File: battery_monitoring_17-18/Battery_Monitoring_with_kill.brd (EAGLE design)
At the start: 50.8 x 127 mm, 57 parts, among them CON4 MOLEX_5566-2, CON5 S3B-PH-SM4-TB, CON6 S3B-PH-SM4-TB, U1 INA3221., U2 INA3221., U4 TEENSY_3.1_BASIC_2, U6 TCAN1042HVDR

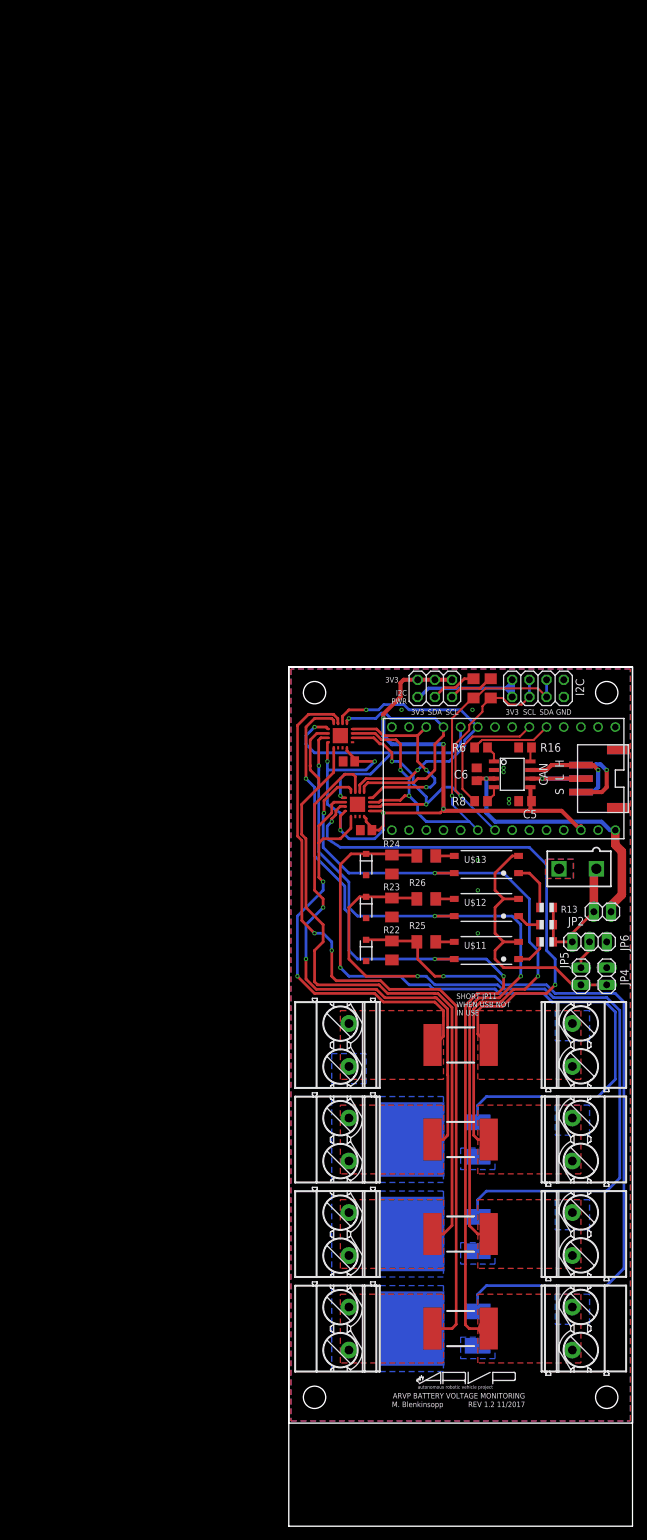
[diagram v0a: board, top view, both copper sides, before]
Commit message: Changed JST connector; Rearranged folders; Generated CAM files
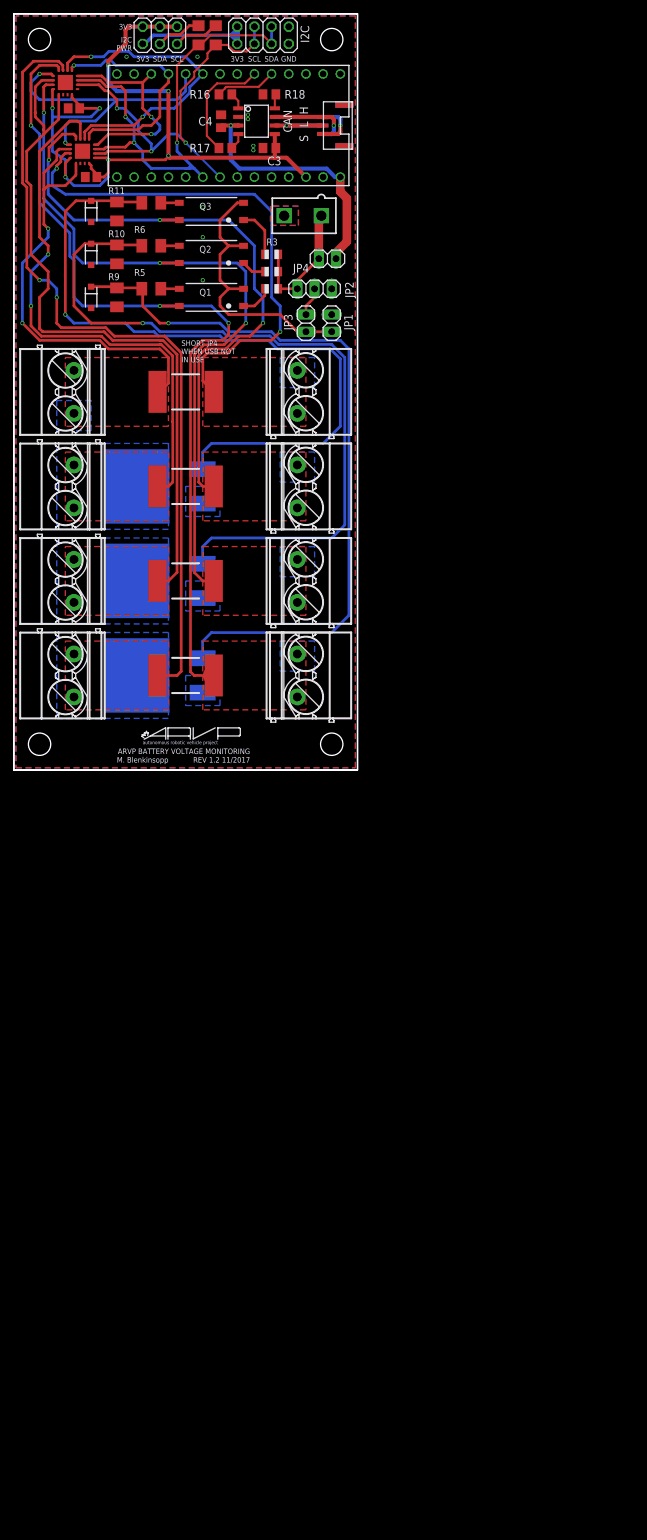
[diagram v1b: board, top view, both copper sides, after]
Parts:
- removed C5, C6: 10u, rcl:C0805
- removed CON4: MOLEX_5566-2, ARVP:5566-2
- removed CON5, CON6: S3B-PH-SM4-TB, ARVP:S3B-PH-SM4-TB
- removed R22, R23, R24: 10k, adafruit:M1206
- removed R25, R26, R27: 1k, adafruit:M1206
- removed U$1, U$2, U$3, U$4, U$5, U$6, U$7, U$8: MKDS_5/2-6,352, Moira:MKDS_5/2-6,35
- removed U$10: ARVP_LOGO, ARVP:ARVP
- removed U$11, U$12, U$13: TCLD1000CT, Moira:SOP-4L
- removed U$14, U$19, U$20: PSMN1R5-30BLE, Moira:SOT404/D2PAK
- removed U$21, U$22, U$23: BZT52C10, Moira:SOD-123
- removed U6: TCAN1042HVDR, ARVP:SO-8
- added ARVP1: ARVP_LOGO, ARVP:ARVP
- added C1: 0.1microF, resistor:C2012
- added C3: 10u, rcl:C0805
- added CON1: MOLEX_5566-2, ARVP:5566-2
- added CON2, CON3: SM03B-GHS-TB, ARVP:SM03B-GHS-TB
- added D1, D2, D3: BZT52C10, Moira:SOD-123
- added J1, J2, J3, J4, J5, J6, J7, J8: MKDS_5/2-6,352, Moira:MKDS_5/2-6,35
- added Q1, Q2, Q3: TCLD1000CT, Moira:SOP-4L
- added Q4, Q5, Q6: PSMN1R5-30BLE, Moira:SOT404/D2PAK
- added R14, R15: 10k, rcl:R1206
- added R17: 220, rcl:R0805
- added R18: 1k, rcl:R0805
- added R2: 1k, adafruit:R0805
- added R5: 1k, adafruit:M1206
- added U$15: (no value), frames:DOCFIELD
- added U$9: (no value), frames:LETTER_P
- added U3: TEENSY_3.1_BASIC_2, Teensy_3_Series_Board_v1.0:TEENSY_3.1_BASIC_2
- C4: value 0.1microF -> 10u; device resistor:C2012 -> rcl:C0805
- JP1: device pinhead:2X03 -> pinhead:1X02
- JP2: device pinhead:1X02 -> pinhead:1X03
- JP3: device pinhead:2X04 -> pinhead:1X02
- JP5: device pinhead:1X02 -> pinhead:2X03
- JP6: device pinhead:1X03 -> pinhead:2X04
- R1, R3: value 0.001Ohm -> 1k; device Moira:3920 -> adafruit:R0805
- R10, R9: device rcl:R1206 -> adafruit:M1206
- R11: value 1k -> 10k; device adafruit:R0805 -> adafruit:M1206
- R12, R13: value 1k -> 0.001Ohm; device adafruit:R0805 -> Moira:3920
- R16: value 1k -> 220
- R6: value 220 -> 1k; device rcl:R0805 -> adafruit:M1206
- R7: value 0.001Ohm -> 1k; device Moira:3920 -> adafruit:M1206
- R8: value 220 -> 0.001Ohm; device rcl:R0805 -> Moira:3920
- U4: value TEENSY_3.1_BASIC_2 -> TCAN1042HVDR; device Teensy_3_Series_Board_v1.0:TEENSY_3.1_BASIC_2 -> ARVP:SO-8
- moved JP5 152.4 mm to (85.1, 179.7), turned to 180 degrees
- moved R1 142.5 mm to (101.6, 142.2), turned to 180 degrees
- moved JP6 142.4 mm to (100.3, 179.7), turned to 180 degrees
- moved R3 133.8 mm to (101.6, 147.3), turned to 180 degrees
- moved R7 132.6 mm to (83.8, 154.9)
- moved R11 125.2 mm to (78.7, 153.7), turned to 90 degrees
- moved R4 117.7 mm to (88.9, 99.1)
- moved JP4 113.8 mm to (109.9, 146.7), turned to 180 degrees
- moved C4 106.9 mm to (94.1, 167.0), turned to 90 degrees
- moved R16 106.2 mm to (94.8, 171.0)
- moved U$24 104.7 mm to (110.5, 74.9)
- moved U$25 104.7 mm to (67.3, 74.9)
- moved U$18 104.7 mm to (110.5, 179.1)
- moved U$26 104.7 mm to (67.3, 179.1)
- moved U1 104.7 mm to (71.1, 172.7)
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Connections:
- net +3V3: now also C1.1, C3.1, JP5.1, JP5.3, JP5.5, U3.3.3V, U4.5; no longer C4.1, C5.1, JP1.1, JP1.3, JP1.5, U4.3.3V, U6.5
- net +5V: now also CON1.1, JP2.1, JP4.2, R1.1, R2.1, R3.1; no longer CON4.1, JP2.2, JP6.1, R11.1, R12.1, R13.1
- net 0-26V_BATTERY1: now also J4.1, Q1.P$4, R8.P$2; no longer R4.P$2, U$1.1, U$11.P$4
- net 0-26V_BATTERY2: now also J3.1, Q2.P$4, R4.P$2; no longer R1.P$2, U$12.P$4, U$2.1
- net 0-26V_BATTERY3: now also J2.1, Q3.P$4, R13.P$2; no longer R3.P$2, U$13.P$4, U$3.1
- net 0-26V_BATTERY4: now also J1.1, R12.P$2; no longer R7.P$2, U$4.1
- net AGND: now also U3.AGND; no longer U4.AGND
- net CANH1: now also CON2.P$3, CON3.P$3, U4.7; no longer CON5.P$3, CON6.P$3, U6.7
- net CANL1: now also CON2.P$2, CON3.P$2, U4.6; no longer CON5.P$2, CON6.P$2, U6.6
- net CANSH1: now also CON2.P$1, CON3.P$1; no longer CON5.P$1, CON6.P$1
- net CAN_RX1: now also R17.2, U4.4; no longer R8.2, U6.4
- net CAN_RX_T: now also R17.1, U3.4; no longer R8.1, U4.4
- net CAN_TX2: now also R16.2, U4.1; no longer R6.2, U6.1
- net CAN_TX_T: now also R16.1, U3.3; no longer R6.1, U4.3
- net CRITICAL_OUT: now also U3.9; no longer U4.9
- net E1: now also Q1.P$3, R5.2; no longer R25.2, U$11.P$3
- net E2: now also Q2.P$3, R6.2; no longer R26.2, U$12.P$3
- net E3: now also Q3.P$3, R7.2; no longer R27.2, U$13.P$3
- net GND: now also C1.2, C3.2, CON1.2, CON2.P$4, CON2.P$5, CON3.P$4, CON3.P$5, D1.P$2, D2.P$2, D3.P$2, J1.2, J2.2, J3.2, J4.2, J8.2, JP1.2, JP2.3, JP6.1, JP6.2, Q4.3S, Q5.3S, Q6.3S, R10.1, R11.1, R18.1, R9.1, U3.GND, U4.2; no longer C5.2, C6.2, CON4.2, CON5.P$4, CON5.P$5, CON6.P$4, CON6.P$5, JP3.1, JP3.2, JP4.2, JP6.3, R16.1, R22.1, R23.1, R24.1, U$1.2, U$14.3S, U$19.3S, U$2.2, U$20.3S, U$21.P$2, U$22.P$2, U$23.P$2, U$3.2, U$4.2, U$8.2, U4.GND, U6.2
- net I2C_3V1: now also JP5.6, JP6.7, JP6.8; no longer JP1.6, JP3.7, JP3.8
- net MD1: now also J5.2, Q4.2D; no longer U$14.2D, U$5.2
- net MD2: now also J6.2, Q5.2D; no longer U$19.2D, U$6.2
- net MD3: now also J7.2, Q6.2D; no longer U$20.2D, U$7.2
- net MG1: now also D1.P$1, Q4.1G, R5.1, R9.2; no longer R22.2, R25.1, U$14.1G, U$21.P$1
- net MG2: now also D2.P$1, Q5.1G, R10.2, R6.1; no longer R23.2, R26.1, U$19.1G, U$22.P$1
- net MG3: now also D3.P$1, Q6.1G, R11.2, R7.1; no longer R24.2, R27.1, U$20.1G, U$23.P$1
- net MOTOR1: now also J5.1, R8.P$1; no longer R4.P$1, U$5.1
- net MOTOR2: now also J6.1, R4.P$1; no longer R1.P$1, U$6.1
- net MOTOR3: now also J7.1, R13.P$1; no longer R3.P$1, U$7.1
- net MOTOR4: now also J8.1, R12.P$1; no longer R7.P$1, U$8.1
- net N$1: now also Q1.P$1, R1.2; no longer R11.2, U$11.P$1
- net N$2: now also Q2.P$1, R2.2; no longer R12.2, U$12.P$1
- net N$3: now also Q3.P$1, R3.2; no longer R13.2, U$13.P$1
- net N$4: now also JP1.1, JP3.1, Q1.P$2, Q2.P$2, Q3.P$2; no longer JP4.1, JP5.1, U$11.P$2, U$12.P$2, U$13.P$2
- net N$5: now also JP2.2, JP3.2; no longer JP5.2, JP6.2
- net PV_OUT: now also U3.7; no longer U4.7
- net SCL: now also JP6.5, JP6.6, R14.2, U3.19/A5; no longer JP3.5, JP3.6, R10.2, U4.19/A5
- net SCL_3V1: now also JP5.2, R14.1; no longer JP1.2, R10.1
- net SDA: now also JP6.3, JP6.4, R15.2, U3.18/A4; no longer JP3.3, JP3.4, R9.2, U4.18/A4
- net SDA_3V1: now also JP5.4, R15.1; no longer JP1.4, R9.1
- net STB1: now also R18.2, U4.8; no longer R16.2, U6.8
- net TC_OUT: now also U3.8; no longer U4.8
- net VIN: now also C4.1, JP4.1, U3.VIN, U4.3; no longer C6.1, JP2.1, U4.VIN, U6.3
- net WARNING_OUT: now also U3.10; no longer U4.10
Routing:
- net SDA: track 70.3 -> 75.7 mm
- net CANSH1: track 10.9 -> 7.34 mm
- net CANH1: track 16.0 -> 12.6 mm
- net CAN_TX_T: track 11.9 -> 9.03 mm
- net VIN: track 41.2 -> 38.3 mm
- net CAN_RX_T: track 19.9 -> 17.0 mm
- net +3V3: track 119.6 -> 118.8 mm
- net CANL1: track 13.2 -> 12.4 mm
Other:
- board size 50.8 x 127 mm -> 50.8 x 111.8 mm
- board text added: "SHORT JP4 WHEN USB NOT IN USE"
- board text removed: "Assumptions: this board is installed in right/rear or left/front section of robot. Teensy USB connector and CAN connector should point towards the center of hull. Mounting holes come from Sparkfun library, located in projects folder. Layout can be changed if needed, as long as USB and CAN guidelines are followed."
- board text removed: "Bottom"
- board text removed: "SHORT JP11 WHEN USB NOT IN USE"
- board text removed: "Towards acrylic wall"
- board text removed: "Towards middle of robot"

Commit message: Fixed issue where motors could still find ground return path even when battery was disconnected by mosfet
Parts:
- moved ARVP1 65.4 mm to (73.7, 139.7), turned to 90 degrees
- moved D1 60.4 mm to (109.5, 91.4), flipped to the bottom
- moved R9 59.5 mm to (111.8, 91.4), flipped to the bottom
- moved D2 53.9 mm to (108.9, 105.4), flipped to the bottom
- moved R10 53.0 mm to (111.1, 105.4), flipped to the bottom
- moved D3 47.1 mm to (108.0, 120.0), flipped to the bottom
- moved R11 46.3 mm to (110.5, 120.0), flipped to the bottom
- moved Q4 8.89 mm to (94.0, 85.1)
- moved Q5 8.89 mm to (94.0, 99.1)
- moved Q6 8.89 mm to (94.0, 113.0)
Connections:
- removed net MD1: J5.2, Q4.2D
- removed net MD2: J6.2, Q5.2D
- removed net MD3: J7.2, Q6.2D
- new net BATT1GND: D1.P$2, J4.1, Q4.3S, R9.1
- new net BATT2GND: D2.P$2, J3.1, Q5.3S, R10.1
- new net BATT3GND: D3.P$2, J2.1, Q6.3S, R11.1
- net 0-26V_BATTERY1: now also J4.2; no longer J4.1
- net 0-26V_BATTERY2: now also J3.2; no longer J3.1
- net 0-26V_BATTERY3: now also J2.2; no longer J2.1
- net 0-26V_BATTERY4: now also J1.2; no longer J1.1
- net GND: now also J1.1, J5.2, J6.2, J7.2, Q4.2D, Q5.2D, Q6.2D; no longer D1.P$2, D2.P$2, D3.P$2, J1.2, J2.2, J3.2, J4.2, Q4.3S, Q5.3S, Q6.3S, R10.1, R11.1, R9.1
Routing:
- net MG3: track 105.1 -> 76.6 mm
- net MG2: track 111.2 -> 83.7 mm
- net MG1: track 108.4 -> 90.8 mm
- net BATT3GND: track 0.00 -> 6.57 mm
- net BATT2GND: track 0.00 -> 6.46 mm
- net BATT1GND: track 0.00 -> 6.27 mm
- net GND: vias 9 -> 25
- added copper zone on layer 16, net BATT1GND
- added copper zone on layer 16, net BATT2GND
- added copper zone on layer 16, net BATT3GND
- removed copper zone on layer 16, net MD1
- removed copper zone on layer 16, net MD2
- removed copper zone on layer 16, net MD3
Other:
- board text added: "+ B -"
- board text added: "+ M -"
- board text added: "+ PB -"
- board text added: "MAX 40A/BATTERY"
- board text added: "REV 1.2 12/2017"
- board text removed: "REV 1.2 11/2017"
